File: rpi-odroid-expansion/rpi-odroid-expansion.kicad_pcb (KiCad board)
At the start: 2 copper layers, 5 parts, among them U1 DS2484R, U2 DS2484R, U3 PCF8563TS, U4 STM32F042K4Tx

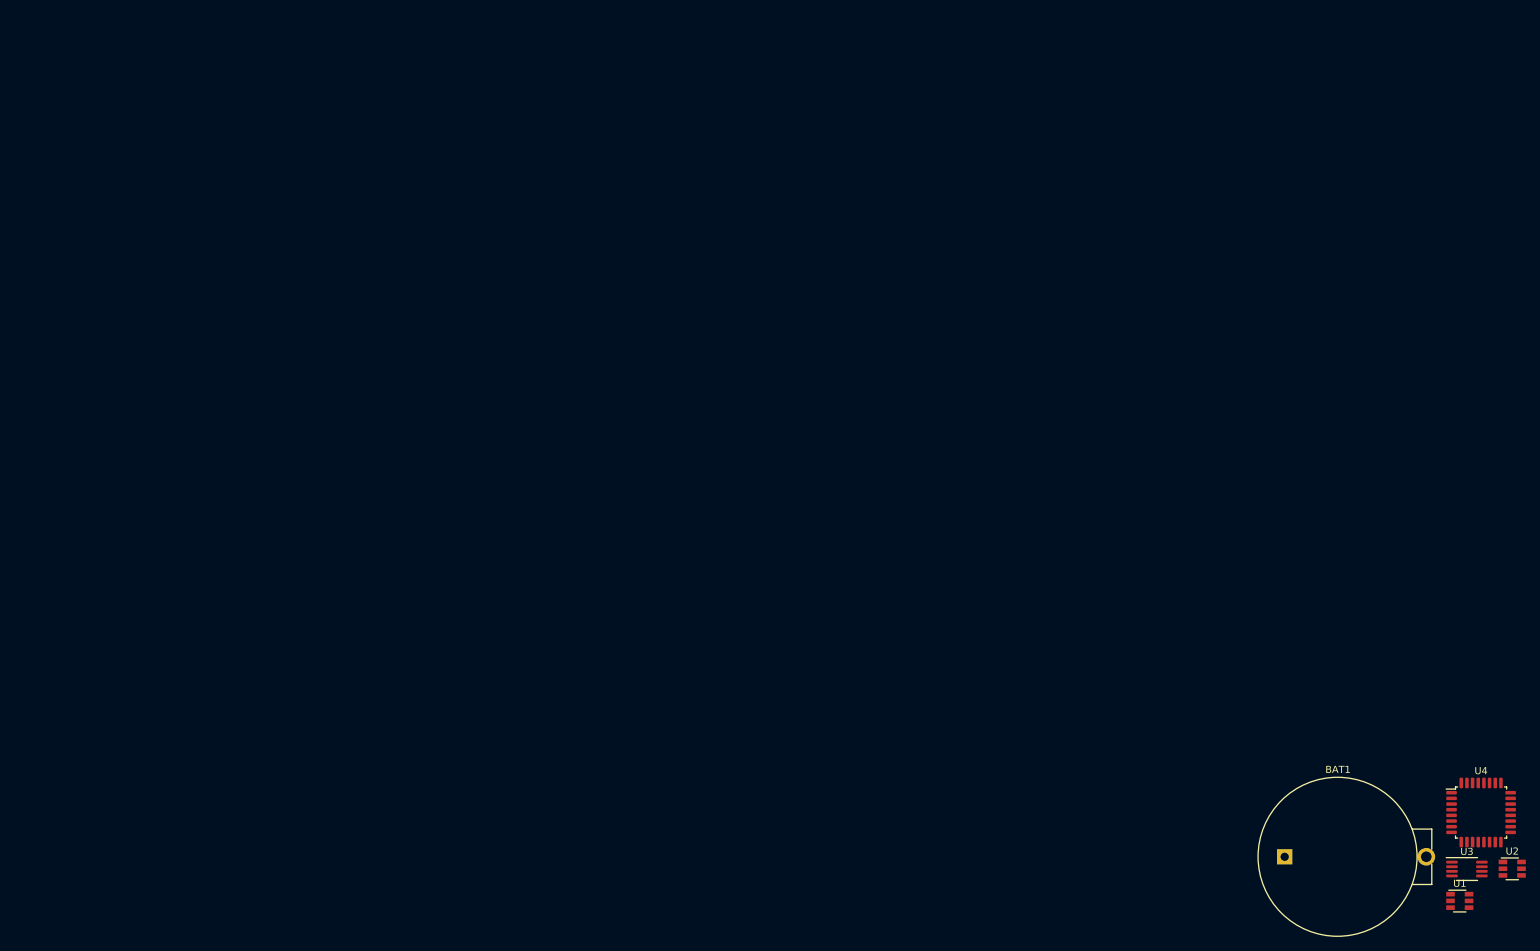
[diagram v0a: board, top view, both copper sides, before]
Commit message: fill in pn's, pull in rPI hat outline, etc
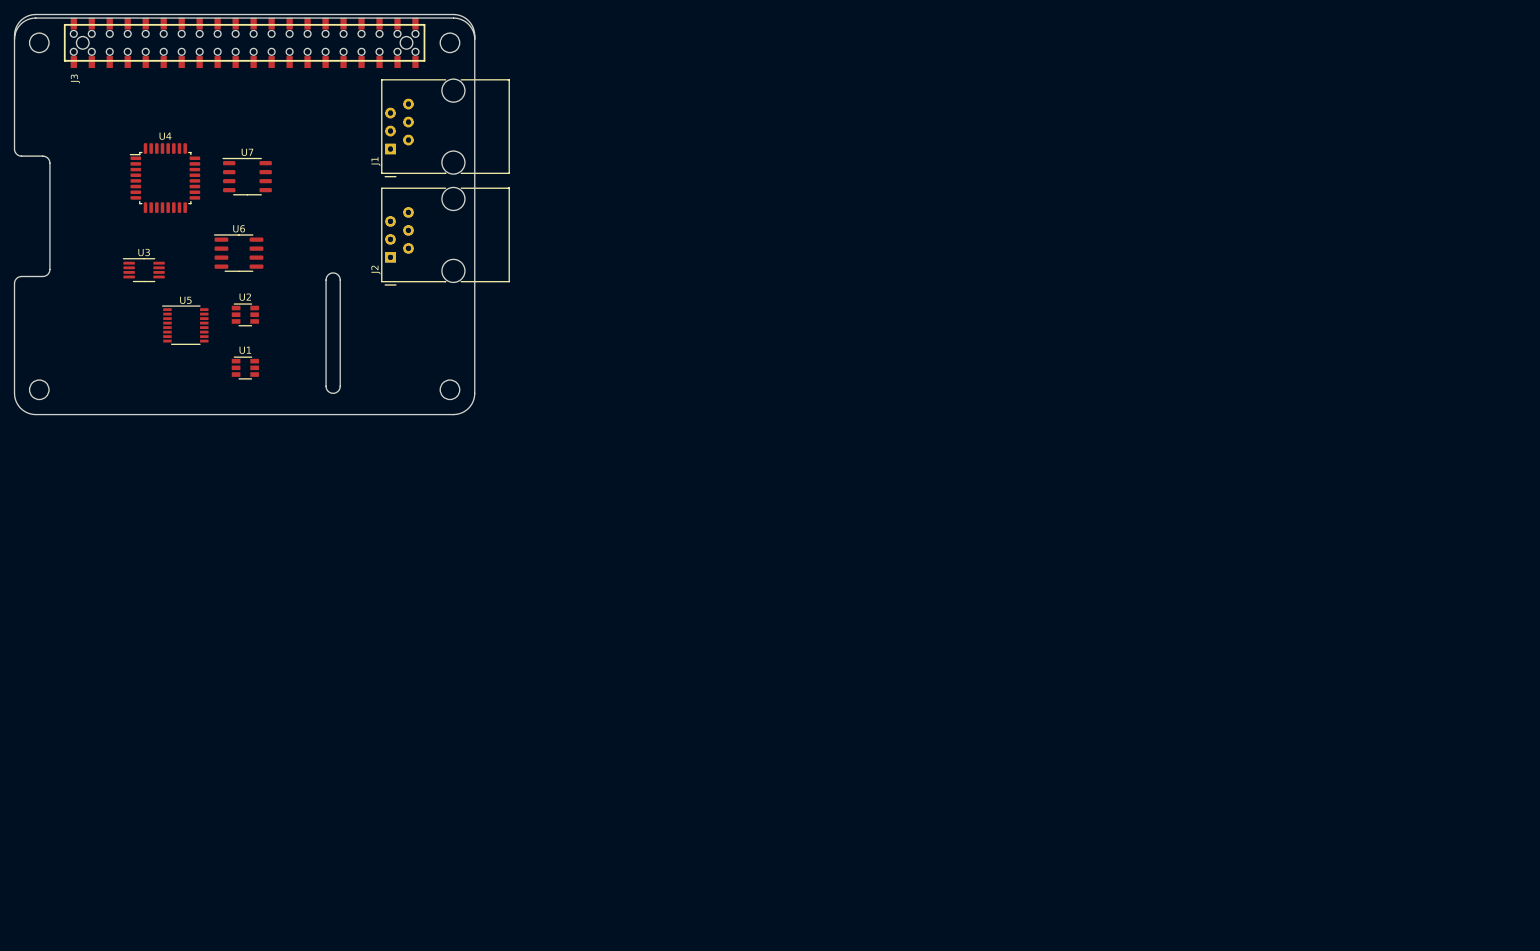
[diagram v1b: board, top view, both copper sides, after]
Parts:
- removed BAT1: Coin, digikey-footprints:Battery_Holder_Coin_2032_BS-7
- added ?: , RPi_Hat:RPi_Hat_Mounting_Hole, F.Cu at (61.5, 4.00)
- added ?: , RPi_Hat:RPi_Hat_Mounting_Hole, F.Cu at (61.5, 53.0)
- added ?: , RPi_Hat:RPi_Hat_Mounting_Hole, F.Cu at (3.50, 53.0)
- added ?: , RPi_Hat:RPi_Hat_Mounting_Hole, F.Cu at (3.50, 4.00)
- added J1: RJ9, Connector_RJ:RJ12_Amphenol_54601, F.Cu at (53.1, 19.0)
- added J2: RJ9, Connector_RJ:RJ12_Amphenol_54601, F.Cu at (53.1, 34.3)
- added J3: rPI_02x20, Simple Iot:Samtec_HLE-120-02-XXX-DV-BE-XX-XX, F.Cu at (32.5, 4.00)
- added U5: TSC2046, Package_SO:SSOP-16_3.9x4.9mm_P0.635mm, F.Cu at (24.2, 43.9)
- added U6: MCP2551-I-SN, Package_SO:SOIC-8_3.9x4.9mm_P1.27mm, F.Cu at (31.7, 33.7)
- added U7: MAX13487E, Package_SO:SO-8_3.9x4.9mm_P1.27mm, F.Cu at (32.9, 22.9)
- U4: value STM32F042K4Tx -> STM32F042K4T6
- moved U4 206.3 mm to (21.3, 23.1)
- moved U3 205.1 mm to (18.3, 36.1)
- moved U2 195.3 mm to (32.6, 42.4)
- moved U1 187.3 mm to (32.6, 49.9)
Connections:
- net Net-(U4-Pad10) renamed /SPI_CS2
- net Net-(U4-Pad14) renamed /GPIO1
- net Net-(U4-Pad15) renamed /GPIO2
- net Net-(U4-Pad26) renamed /GPIO3
- net Net-(U4-Pad27) renamed /GPIO4
- U4 pad 11: Net-(U4-Pad11) -> /SPI_CLK
- U4 pad 12: Net-(U4-Pad12) -> /SPI_MOSI
- U4 pad 13: Net-(U4-Pad13) -> /SPI_MISO
- U4 pad 19: Net-(U4-Pad19) -> /RS485_TX
- U4 pad 20: Net-(U4-Pad20) -> /RS485_RX
- U4 pad 21: Net-(U4-Pad21) -> /CAN_RX
- U4 pad 22: Net-(U4-Pad22) -> /CAN_TX
- U4 pad 28: Net-(U4-Pad28) -> /GPIO5
- U4 pad 29: Net-(U4-Pad29) -> /ID_SCL
- U4 pad 30: Net-(U4-Pad30) -> /ID_SDA
- U4 pad 4: Net-(U4-Pad4) -> /MCU_RSTn
- U4 pad 8: Net-(U4-Pad8) -> /UART_RX
- U4 pad 9: Net-(U4-Pad9) -> /UART_TX
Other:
- board outline added: 65 x 56.5 mm
- net class Default: via_dia 0.8 -> 0.6
- rule pad_to_mask_clearance: 0.05 -> 0
- rule trace_min: 0.2 -> 0.01
- board text added: "Camera Flex Slot (Optional)"
- board text added: "Dimensions taken from https://github.com/raspberrypi/hats/blob/master/hat-board-mechanical.pdf"
- board text added: "Select one of these board edges depending upon the type of socket that is used."
